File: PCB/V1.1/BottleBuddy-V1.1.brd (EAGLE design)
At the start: 100 x 99.7 mm, 55 parts, among them Q1 MOSFET-PCHANNEL, Q2 MOSFET-PCHANNEL, Q3 200mA/50V, U1 74AHC1G125, U2 MAX1704X, U3 MMA8452Q, U4 BME280, U5 MCKPT-G1210-3916

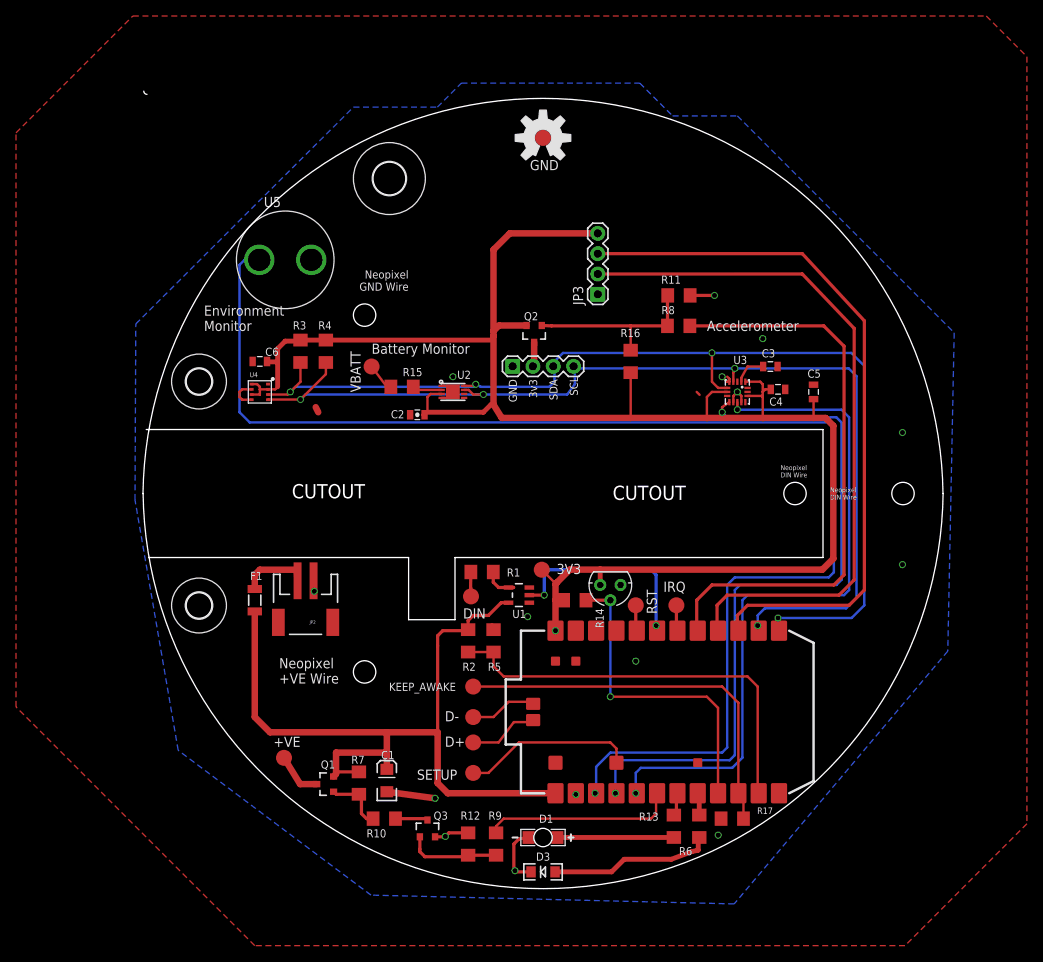
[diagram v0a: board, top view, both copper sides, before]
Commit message: Modified V1.1 to use plug-in modules for Accelerometer and BME280 to make life easier.
Removed one LED.

Changed keep awake, moved DB18B20 so it can be close to the load cell and possibly fixed as it's by the fixed part.
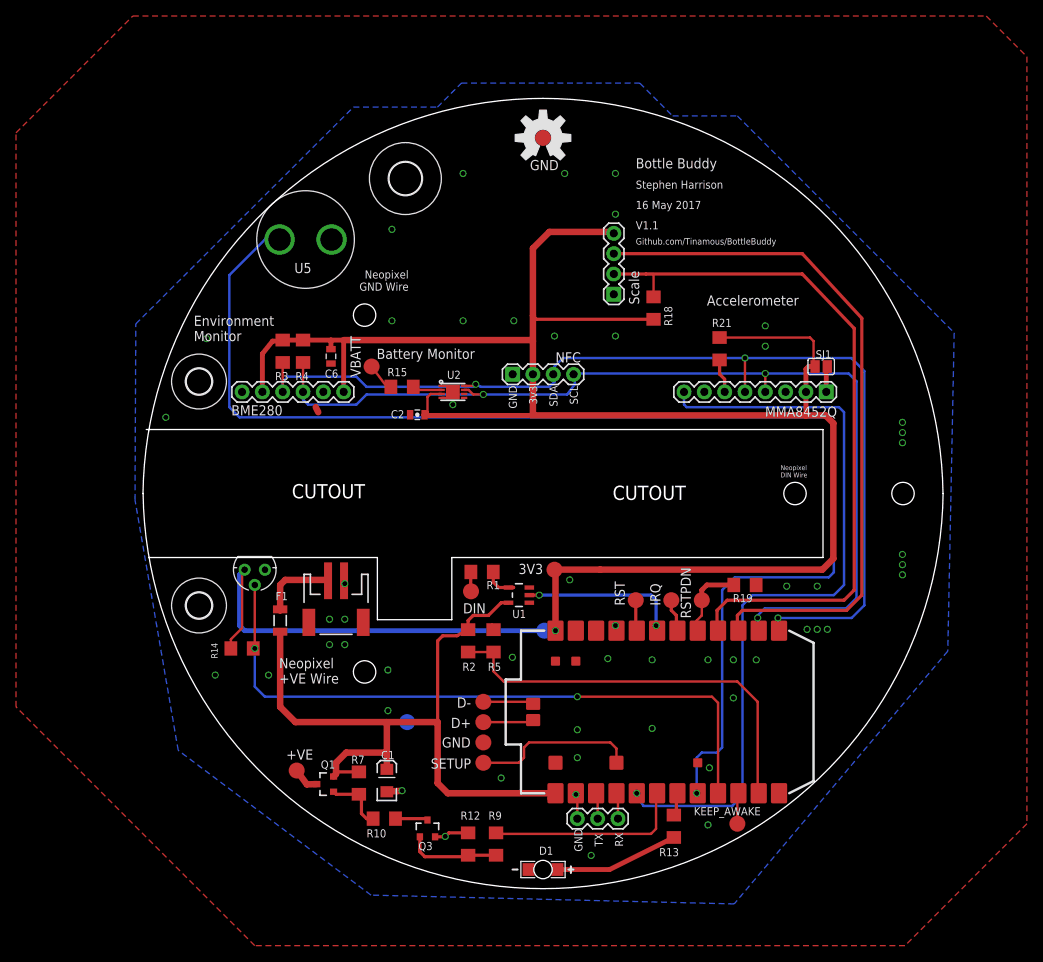
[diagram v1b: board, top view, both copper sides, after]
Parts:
- removed C3, C5: 0.1uF, SparkFun-Capacitors:0805
- removed C4: 4.7uF, SparkFun-Capacitors:0805
- removed D3: RED, SparkFun-LED:LED-1206
- removed Q2: MOSFET-PCHANNEL, SparkFun-DiscreteSemi:SOT23-3
- removed R11: DNP, SparkFun-Resistors:1206
- removed R16: 10k, SparkFun-Resistors:1206
- removed R17: 100k, SparkFun-Resistors:1206
- removed R6: 1k5, SparkFun-Resistors:1206
- removed R8: 100r, SparkFun-Resistors:1206
- removed U3: MMA8452Q, SparkFun-Sensors:QFN-16_0.5MM
- removed U4: BME280, SparkFun-Sensors:LGA-8-2.5X2.5
- added 3V3_LOWER_TP, GND24, GND_LOWER_TP: TPTP20R, testpad:TP20R
- added BME280: (no value), SparkFun-Connectors:1X06
- added JP1: (no value), SparkFun-Connectors:1X03
- added LOGO1: OSHW-LOGOL, SparkFun-Aesthetics:OSHW-LOGO-L
- added MMA8452Q: (no value), SparkFun-Connectors:1X08
- added R18: 10k, SparkFun-Resistors:1206
- added R19: 2k2, SparkFun-Resistors:1206
- added R21: DNP, SparkFun-Resistors:1206
- added RSTPDN: NFC IRQ, testpad:TP20R
- added SJ1: (no value), jumper:SJ
- R1, R9: value 100r -> 100R
- R10: value 10k -> 1k
- R12: value 10k -> 1M
- R2, R5: value (none) -> 30k
- moved S1 44.5 mm to (14.0, -9.53)
- moved R14 42.0 mm to (12.4, -19.4)
- moved KEEP_AWAKE 37.2 mm to (74.3, -41.3)
- moved C6 8.91 mm to (23.5, 17.1), turned to 270 degrees
- moved F1 4.07 mm to (17.1, -15.9)
- moved D1 4.00 mm to (50.0, -47.0)
- moved JP2 3.81 mm to (24.1, -14.6)
- moved U5 3.59 mm to (20.3, 31.8)
- moved R4 2.86 mm to (20.0, 17.8)
- moved D+ 2.84 mm to (42.5, -28.6)
- moved D- 2.29 mm to (42.5, -26.0)
- moved +VE 2.25 mm to (19.2, -34.6)
- moved R3 2.22 mm to (17.5, 17.8)
- moved H3 2.00 mm to (32.8, 39.4)
- moved JP3 2.00 mm to (58.9, 24.9)
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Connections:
- removed net INT2: U$1.4, U3.9
- removed net N$13: D3.A, R6.2
- removed net N$8: R6.1, U$1.8
- removed net NFC_POWER: Q2.1, R11.2, R16.1, R8.2
- new net N$20: MMA8452Q.6, R21.2
- new net RSTPDN: R19.2, RSTPDN.TP, U$1.17
- net 3.3V: now also 3V3_LOWER_TP.TP, BME280.2, BME280.6, JP5.2, MMA8452Q.2, R18.1, R21.1, SJ1.2; no longer C4.1, C5.1, Q2.2, R16.2, U3.1, U3.14, U3.7, U4.2, U4.6, U4.8
- net BUZZER: now also U$1.8; no longer U$1.3
- net GND: now also BME280.1, BME280.5, GND24.TP, GND_LOWER_TP.TP, JP1.1, MMA8452Q.3, R19.1; no longer C3.2, C4.2, C5.2, D3.C, R11.1, R17.2, U3.10, U3.12, U3.5, U4.1, U4.5, U4.7
- net INT1: now also MMA8452Q.8; no longer U3.11
- net N$12: no longer R17.1
- net N$18: now also MMA8452Q.1, SJ1.1; no longer C3.1, U3.2
- net N$4: now also JP1.3, U$1.4; no longer JP5.2, Q2.3
- net N$7: now also JP1.2, U$1.3; no longer R8.1, U$1.17
- net SCALE_CLOCK: now also R18.2
- net SCL: now also BME280.4, MMA8452Q.4; no longer U3.4, U4.4
- net SDA: now also BME280.3, MMA8452Q.5; no longer U3.6, U4.3
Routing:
- net INT2: track 90.6 -> 0.00 mm, vias 2 -> 0
- net 3.3V: track 223.0 -> 292.3 mm
- net N$7: track 72.5 -> 3.25 mm
- net N$12: track 48.7 -> 3.86 mm
- net DQ: track 39.8 -> 83.3 mm, vias 1 -> 2
- net NFC_POWER: track 22.6 -> 0.00 mm
- net GND: track 36.2 -> 15.4 mm, vias 15 -> 54
- net N$13: track 20.5 -> 0.00 mm
- net INT1: track 87.4 -> 97.6 mm, vias 2 -> 1
- net RSTPDN: track 0.00 -> 9.66 mm
- net BUZZER: track 170.0 -> 162.6 mm
- net VIN: track 99.9 -> 93.0 mm
- net SCL: track 130.7 -> 124.5 mm, vias 4 -> 3
- net NEOPIXELS: track 25.9 -> 20.0 mm
- net N$20: track 0.00 -> 4.26 mm
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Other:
- board size 100 x 99.7 mm -> 100 x 98.8 mm
- board text added: "16 May 2017"
- board text added: "Bottle Buddy"
- board text added: "Github.com/Tinamous/BottleBuddy"
- board text added: "RX"
- board text added: "Stephen Harrison"
- board text added: "TX"
- board text added: "V1.1"
